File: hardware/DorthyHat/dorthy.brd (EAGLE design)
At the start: 100 x 80 mm, 25 parts, among them J1 90325-0004, J2 90325-0004, U2 DEV-15583

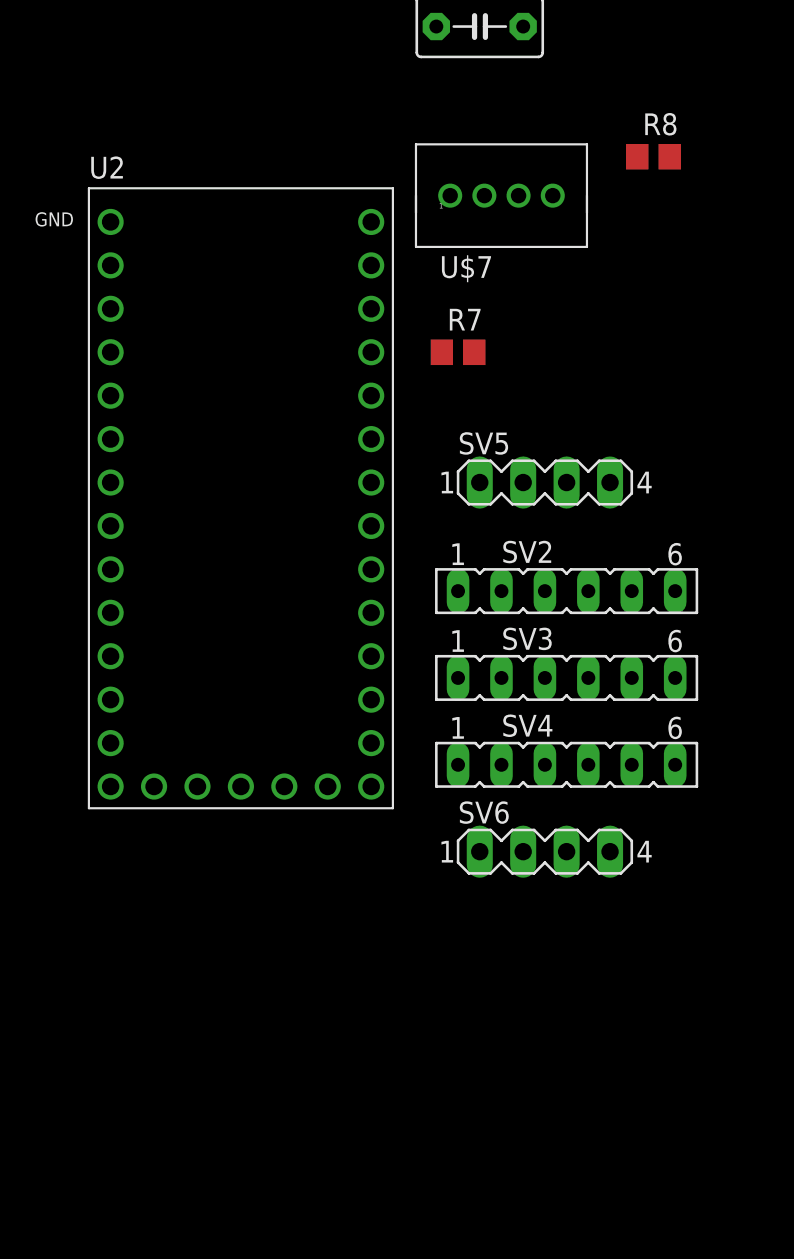
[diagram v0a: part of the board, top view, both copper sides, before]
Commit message: added touch screen lcd to dorthy, realized teensy 4.0 does not have true analog outputs, need to revert to 3.5 if I want simple outs...
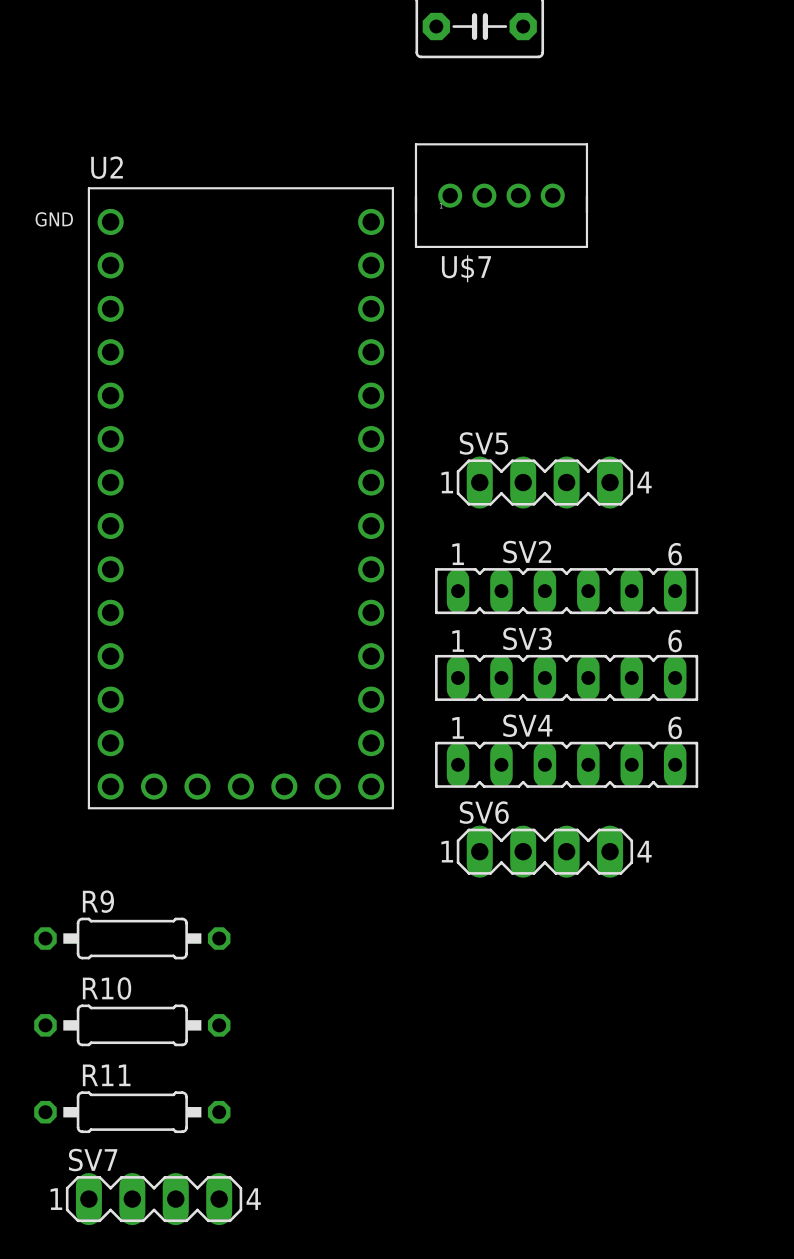
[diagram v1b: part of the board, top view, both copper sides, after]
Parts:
- removed R7: 10k, rcl:R0805
- removed R8: 10K, rcl:R0805
- added R10, R11: 10K, rcl:0207/10
- added R9: 100, rcl:0207/10
- added SV7: (no value), con-lstb:MA04-1
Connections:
- new net LED: JP1.8, R9.2
- net GND: now also SV7.1
- net LA: no longer U2.15
- net RA: no longer U2.14
- net SCL: now also R10.2, SV7.4; no longer R7.2
- net SDA: now also R11.2, SV7.3; no longer R8.2
- net VCC: now also R9.1; no longer JP1.8
- net VEE: now also R10.1, R11.1, SV7.2; no longer R7.1, R8.1

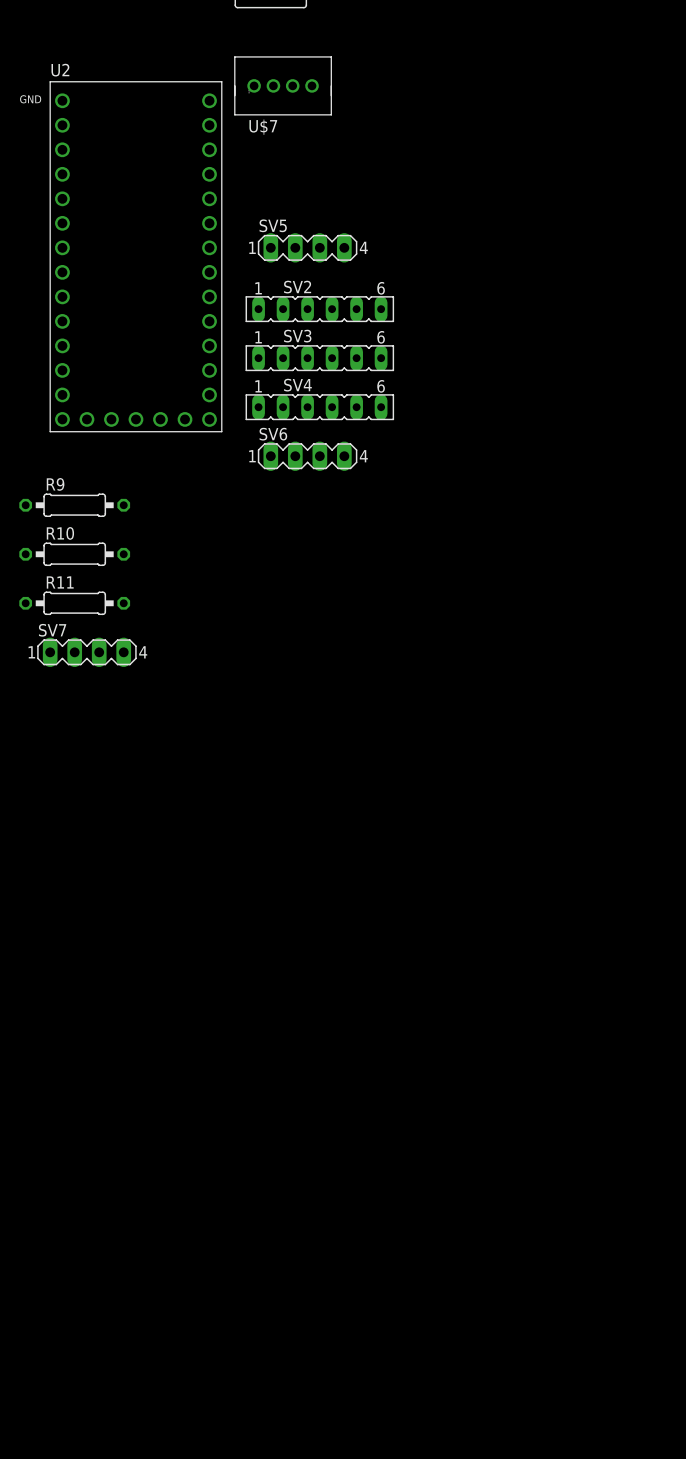
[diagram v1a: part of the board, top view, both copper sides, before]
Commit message: change to teensy 3.6. Add AGND for audio outs. Add power headers for future addons
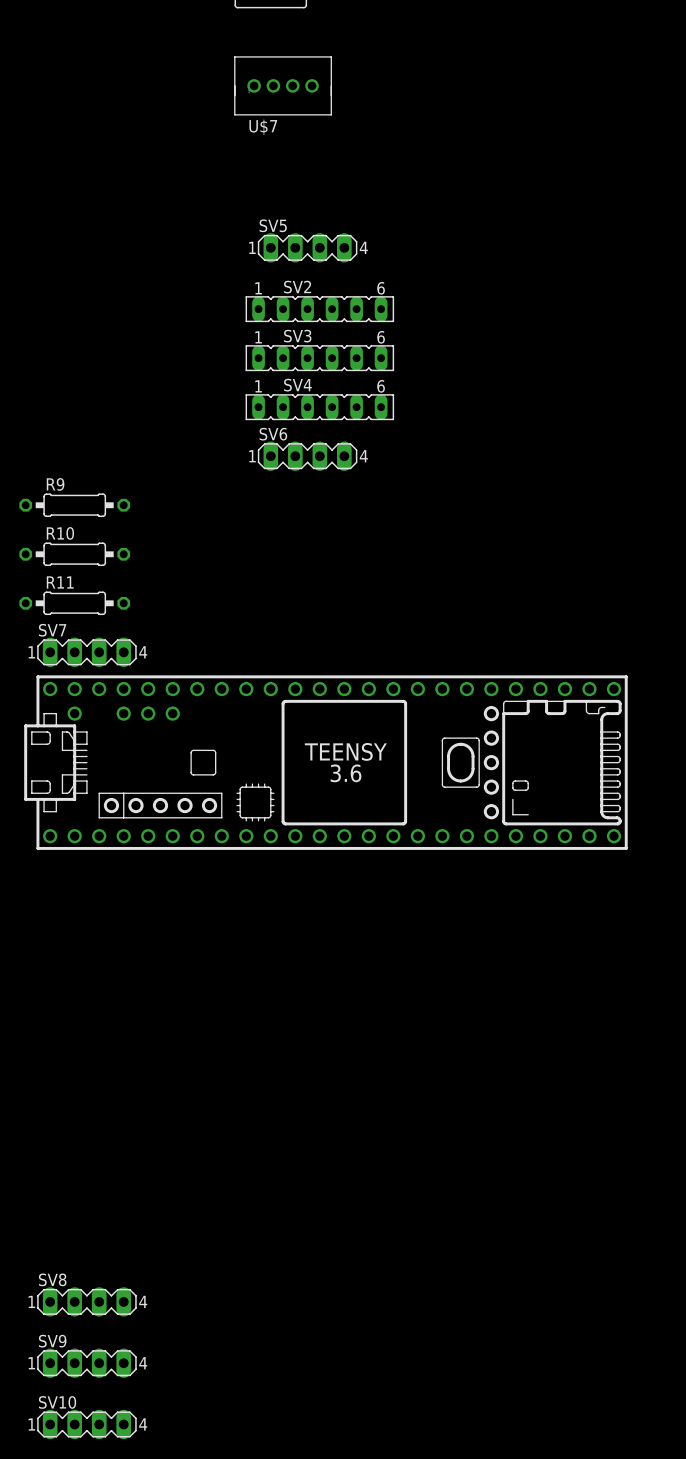
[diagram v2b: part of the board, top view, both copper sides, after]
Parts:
- removed U2: DEV-15583, DEV-15583:MODULE_DEV-15583
- added SV10, SV8, SV9: (no value), con-lstb:MA04-1
- added U$1: TEENSY_3.5/3.6_BASIC, Teensy356:TEENSY_3.5/3.6_BASIC
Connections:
- removed net VBAT: U2.VBAT
- new net AGND: SV10.1, SV6.1, SV6.3, SV8.1, SV8.3, SV9.1, U$1.AGND
- net CS: now also U$1.10/CS; no longer U2.10
- net D/C: now also U$1.9/CS; no longer U2.9
- net GND: now also SV10.2, SV9.2, U$1.GND; no longer U2.G1, U2.G2, U2.G3
- net LA: now also U$1.A22/DAC1
- net LABYPASS: now also SV8.2; no longer SV6.1
- net MIDIRX: now also U$1.0/RX; no longer U2.0
- net MIDITX: now also U$1.1/TX; no longer U2.1
- net O3A: now also U$1.3/CANTX; no longer U2.3
- net O4A: now also U$1.4/CANRX; no longer U2.4
- net RA: now also U$1.21/DAC0
- net RABYPASS: now also SV8.4; no longer SV6.3
- net SCK: now also U$1.13/SCK; no longer U2.13
- net SCL: now also U$1.19/A5/SCL; no longer U2.19
- net SDA: now also U$1.18/A4/SDA; no longer U2.18
- net SDI: now also U$1.11/MOSI; no longer U2.11
- net SDO: now also U$1.12/MISO; no longer U2.12
- net TCS: now also U$1.21/A7; no longer U2.8
- net TIRQ: now also U$1.2; no longer U2.2
- net VCC: now also SV10.4, SV9.4, U$1.VIN, U$1.VUSB; no longer U2.VIN
- net VEE: now also SV10.3, SV9.3, U$1.3V3, U$1.3V3_LO; no longer U2.3.3V_1, U2.3.3V_2

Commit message: make board 100mmX100mm. add 9 capacitive touch pads. add rotary encoder... why not?
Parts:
- added MT1: PEC11R-4215F-S0024, PEC11R-4215F-S0024:XDCR_PEC11R-4215F-S0024
- added TP$1, TP$2, TP$3, TP$4, TP$5, TP$6, TP$7, TP$8, TP$9: CAPACITIVE_TOUCH_PAD, CRcustom:CAP_PAD1
- moved C1 492.7 mm to (-30.5, -632.5)
- moved C3 485.9 mm to (-22.9, -632.5)
- moved U$7 461.0 mm to (-29.2, -616.0)
- moved SV5 453.4 mm to (-26.7, -626.1)
- moved SV6 445.8 mm to (-26.7, -640.1)
- moved R9 397.7 mm to (-27.9, -598.2)
- moved SV8 363.4 mm to (-26.7, -646.4)
- moved SV10 313.9 mm to (-26.7, -609.6)
- moved SV9 313.9 mm to (-26.7, -603.2)
- moved U$1 283.5 mm to (-3.81, -510.5)
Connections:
- new net EA: MT1.A, U$1.6
- new net EB: MT1.B, U$1.7
- new net P1: TP$1.P$1, U$1.23/A9
- new net P2: TP$2.P$1, U$1.22/A8
- new net P3: TP$3.P$1, U$1.17/A3
- new net P4: TP$4.P$1, U$1.16/A2
- new net P5: TP$5.P$1, U$1.15/A1
- new net P6: TP$6.P$1, U$1.29
- new net P7: TP$7.P$1, U$1.30
- new net P8: TP$8.P$1, U$1.19/A5/SCL
- new net P9: TP$9.P$1, U$1.18/A4/SDA
- new net SW1: MT1.1, U$1.5
- net GND: now also MT1.2, MT1.COM, MT1.S1, MT1.S2
- net O3A: no longer U$1.3/CANTX
- net O4A: no longer U$1.4/CANRX
- net SCL: now also U$1.3/CANTX; no longer U$1.19/A5/SCL
- net SDA: now also U$1.4/CANRX; no longer U$1.18/A4/SDA
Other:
- board size 100 x 80 mm -> 100 x 100 mm

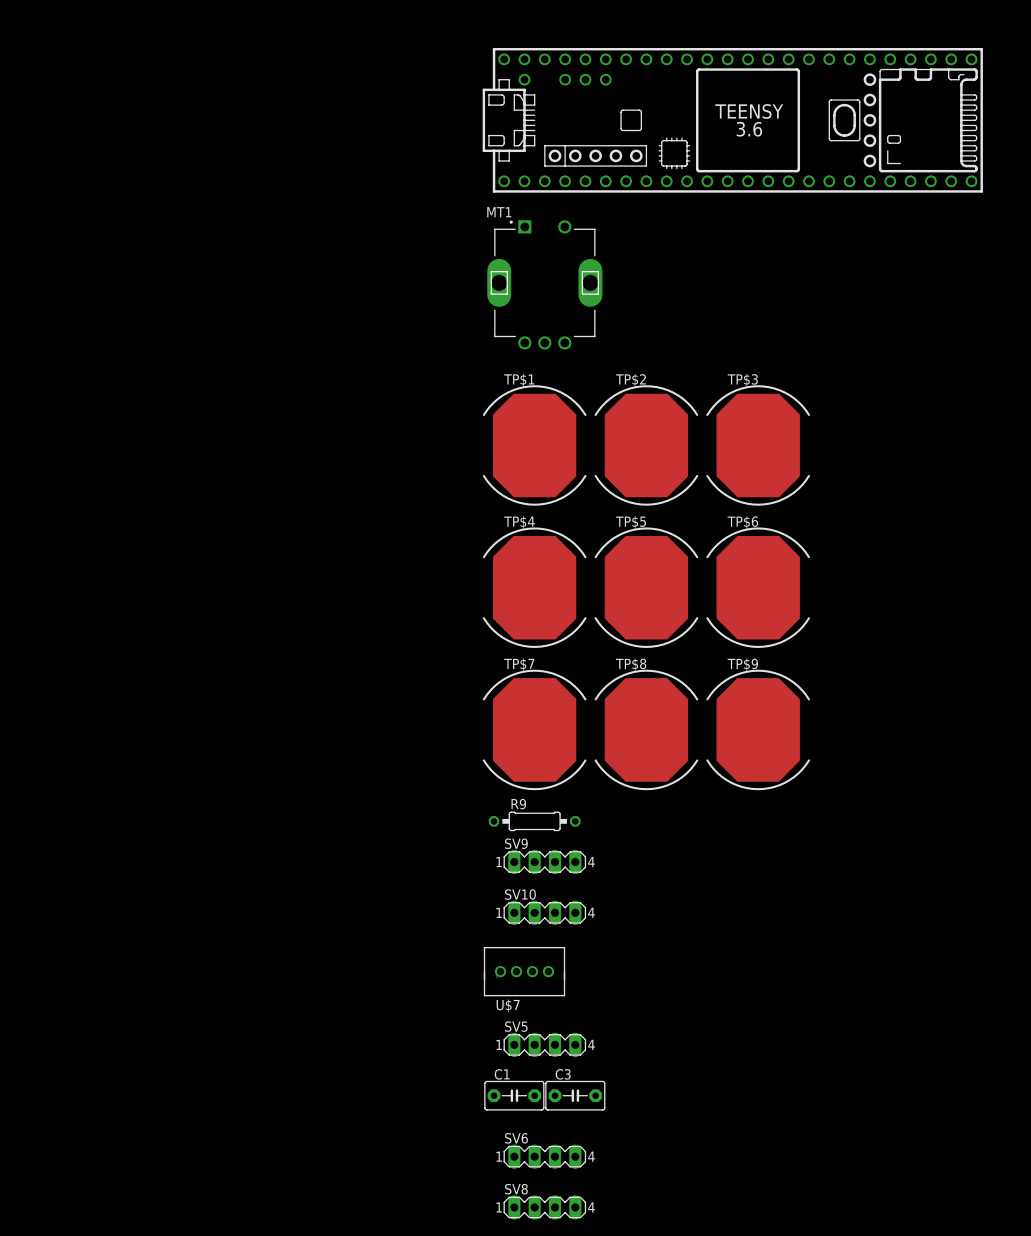
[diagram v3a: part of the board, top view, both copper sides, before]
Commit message: change shematic (back) to teensy 4.0, with audio sheild and touch display
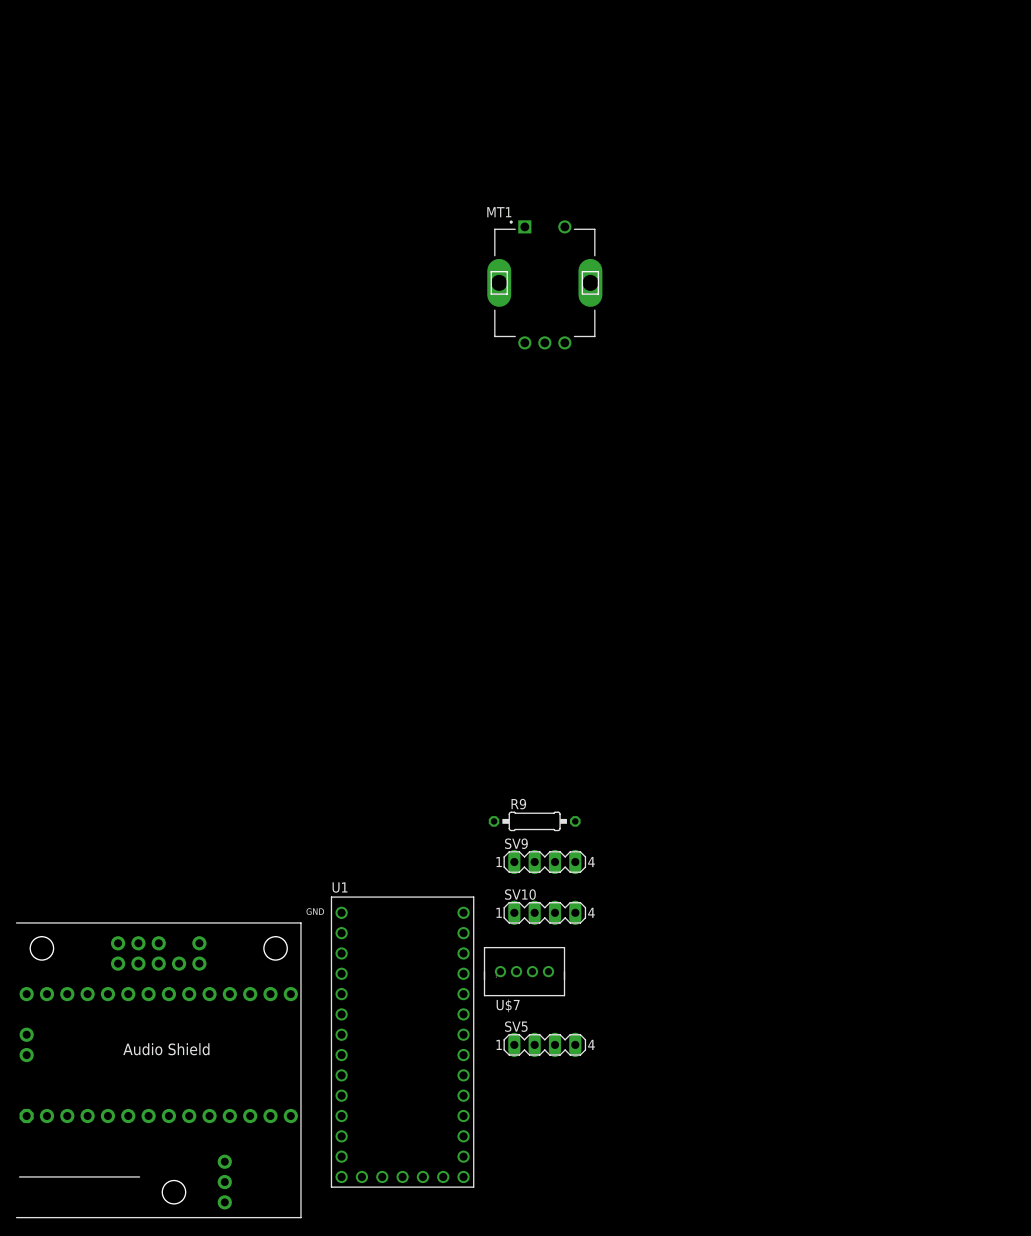
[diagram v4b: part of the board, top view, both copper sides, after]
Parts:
- removed C1, C3: 1uf, capacitor-wima:C5B3.5
- removed SV6, SV8: (no value), con-lstb:MA04-1
- removed TP$1, TP$2, TP$3, TP$4, TP$5, TP$6, TP$7, TP$8, TP$9: CAPACITIVE_TOUCH_PAD, CRcustom:CAP_PAD1
- removed U$1: TEENSY_3.5/3.6_BASIC, Teensy356:TEENSY_3.5/3.6_BASIC
- added U$2: AUDIOSHIELD-REVD, Teensy_Audioshield:AUDIOSHIELD-REVD
- added U1: DEV-15583, DEV-15583:MODULE_DEV-15583
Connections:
- removed net AGND: SV10.1, SV6.1, SV6.3, SV8.1, SV8.3, SV9.1, U$1.AGND
- removed net LA: C1.1, U$1.A22/DAC1
- removed net LABYPASS: C1.2, SV6.2, SV8.2
- removed net P1: TP$1.P$1, U$1.23/A9
- removed net P2: TP$2.P$1, U$1.22/A8
- removed net P3: TP$3.P$1, U$1.17/A3
- removed net P4: TP$4.P$1, U$1.16/A2
- removed net P5: TP$5.P$1, U$1.15/A1
- removed net P6: TP$6.P$1, U$1.29
- removed net P7: TP$7.P$1, U$1.30
- removed net P8: TP$8.P$1, U$1.19/A5/SCL
- removed net P9: TP$9.P$1, U$1.18/A4/SDA
- removed net RA: C3.1, U$1.21/DAC0
- removed net RABYPASS: C3.2, SV6.4, SV8.4
- new net BCLK: U$2.21, U1.21
- new net DIN: U$2.7, U1.7
- new net DOUT: U$2.8, U1.8
- new net LCLK: U$2.20, U1.20
- new net MCLK: U$2.23, U1.23
- new net MEMCS: U$2.6, U1.6
- new net SDCS: U$2.10, U1.10
- new net VBAT: U1.VBAT
- new net VOL: U$2.15, U1.16
- net CS: now also U1.15; no longer U$1.10/CS
- net D/C: now also U1.9; no longer U$1.9/CS
- net EA: now also U1.4; no longer U$1.6
- net EB: now also U1.5; no longer U$1.7
- net GND: now also SV10.1, SV9.1, U$2.G, U$2.GND, U1.G1, U1.G2, U1.G3; no longer U$1.GND
- net MIDIRX: now also U1.0; no longer U$1.0/RX
- net MIDITX: now also U1.1; no longer U$1.1/TX
- net SCK: now also U$2.13, U1.13; no longer U$1.13/SCK
- net SCL: now also U$2.19, U1.19; no longer U$1.3/CANTX
- net SDA: now also U$2.18, U1.18; no longer U$1.4/CANRX
- net SDI: now also U$2.11, U1.11; no longer U$1.11/MOSI
- net SDO: now also U$2.12, U1.12; no longer U$1.12/MISO
- net SW1: now also U1.3; no longer U$1.5
- net TCS: now also U1.14; no longer U$1.21/A7
- net TIRQ: now also U1.2; no longer U$1.2
- net VCC: now also U$2.5V, U1.VIN; no longer U$1.VIN, U$1.VUSB
- net VEE: now also U$2.3V, U1.3.3V_1, U1.3.3V_2; no longer U$1.3V3, U$1.3V3_LO

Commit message: add custom footprint for the display
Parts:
- removed JP1: (no value), pinhead:1X14
- added U$1: ILI9341, ili9341:ILI9341
- moved U$2 658.4 mm to (20.3, 21.6), turned to 90 degrees
- moved U1 654.7 mm to (50.8, 21.6), turned to 180 degrees
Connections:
- net CS: now also U$1.CS; no longer JP1.3
- net D/C: now also U$1.DC; no longer JP1.5
- net GND: now also U$1.GND; no longer JP1.2
- net LED: now also U$1.LED; no longer JP1.8
- net SCK: now also U$1.SCK, U$1.TCLK; no longer JP1.10, JP1.7
- net SDI: now also U$1.SDI, U$1.TDIN; no longer JP1.12, JP1.6
- net SDO: now also U$1.SDO, U$1.TDO; no longer JP1.13, JP1.9
- net TCS: now also U$1.TCS; no longer JP1.11
- net TIRQ: now also U$1.TIRQ; no longer JP1.14
- net VCC: now also U$1.VCC; no longer JP1.1
- net VEE: now also U$1.RST; no longer JP1.4

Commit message: start moving components around
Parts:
- moved SV5 705.7 mm to (8.89, 78.7)
- moved U$7 704.6 mm to (8.89, 87.6)
- moved SV10 696.1 mm to (58.4, 81.3)
- moved SV9 696.1 mm to (58.4, 87.6)
- moved R9 679.3 mm to (72.4, 73.7)
- moved MT1 597.3 mm to (33.0, 63.5)
- moved SV7 312.1 mm to (21.6, 94.0)
- moved R10 291.0 mm to (22.9, 82.5)
- moved R11 291.0 mm to (22.9, 77.5)
- moved SV4 210.9 mm to (73.7, 10.2)
- moved SV3 202.4 mm to (73.7, 6.35)
- moved SV1 196.1 mm to (21.6, 88.9)
- moved SV2 194.0 mm to (73.7, 2.54)
- moved C2 193.7 mm to (50.8, 55.9)
- moved J1 147.7 mm to (83.8, 40.6), turned to 270 degrees
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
